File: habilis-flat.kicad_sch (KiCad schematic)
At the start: 73 parts, among them J1 AudioJack4, SW1 MX, SW10 MX, SW11 MX, SW12 MX, SW13 MX, SW14 MX, SW15 MX, SW16 MX, SW17 MX, SW18 MX, SW19 MX, SW2 MX, SW20 MX, SW21 MX, SW22 MX, SW23 MX, SW24 MX, SW25 MX, SW26 MX, SW27 MX, SW28 MX, SW29 MX, SW3 MX, SW31 MX, SW32 MX, SW33 MX, SW34 MX, SW35 MX, SW36 MX, SW4 MX, SW5 MX, SW6 MX, SW7 MX, SW8 MX, SW9 MX, U1 ProMicro

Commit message: Revision 1
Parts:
- removed D36: 1N4148, Diode_THT:D_DO-35_SOD27_P7.62mm_Horizontal, symbol Diode:1N4148
- added D35: 1N4148, Diode_THT:D_DO-35_SOD27_P7.62mm_Horizontal, symbol Diode:1N4148
- renumbered D31 to D30, D32 to D31, D33 to D32, D34 to D33, D35 to D34, SW31 to SW30, SW32 to SW31, SW33 to SW32, SW34 to SW33, SW35 to SW34, SW36 to SW35
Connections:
- net at D14.1 (K), D19.1 (K), D24.1 (K)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: now also D34.1 (K); no longer D33.1 (K)
- net at D10.1 (K), D15.1 (K), D20.1 (K)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: now also D30.1 (K), D35.1 (K); no longer D34.1 (K)
- net at SW26.2, SW27.2, SW28.2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: now also SW30.2
- net at D1.1 (K), D11.1 (K), D16.1 (K)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: now also D31.1 (K); no longer D30.1 (K)
- net at J1.S: no longer U1.5 (SDA)
- net at SW31.2, SW32.2, SW34.2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: now also SW33.1, U1.18 (F6); no longer SW30.2, SW33.2, U1.19 (F5)
- net at D12.1 (K), D17.1 (K), D2.1 (K)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: now also D32.1 (K); no longer D31.1 (K)
- net at SW35.1: now also D35.2 (A)
- net at D13.1 (K), D18.1 (K), D23.1 (K)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: now also D33.1 (K); no longer D32.1 (K)
- net at D33.2 (A): now also SW33.2; no longer SW33.1
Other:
- moved on the sheet: D30, D31, D32, D33, D34, SW30, SW31, SW32, SW33, SW34, SW35

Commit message: Revision 2
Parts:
- J1: footprint Connector_PinHeader_2.54mm:PinHeader_1x04_P2.54mm_Vertical -> project-components:Jack breakout board
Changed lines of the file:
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@@
       (effects (font (size 1.27 1.27)))
     )
-    (property "Footprint" "Connector_PinHeader_2.54mm:PinHeader_1x04_P2.54mm_Vertical" (at 85.09 120.65 0)
+    (property "Footprint" "project-components:Jack breakout board" (at 85.09 120.65 0)
       (effects (font (size 1.27 1.27)) hide)
     )

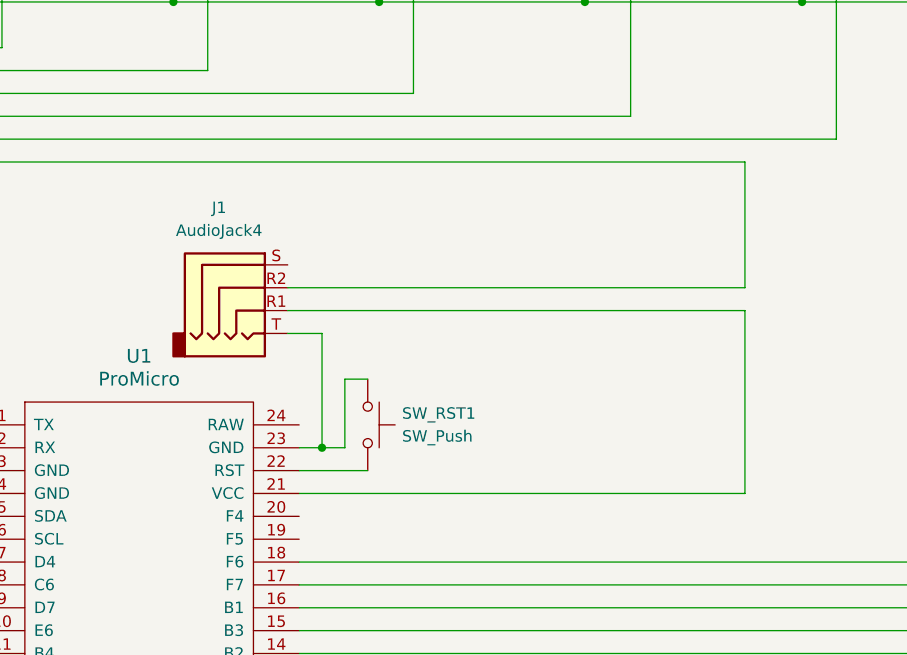
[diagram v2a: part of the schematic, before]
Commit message: Merge R1 and R2 of the TRRS
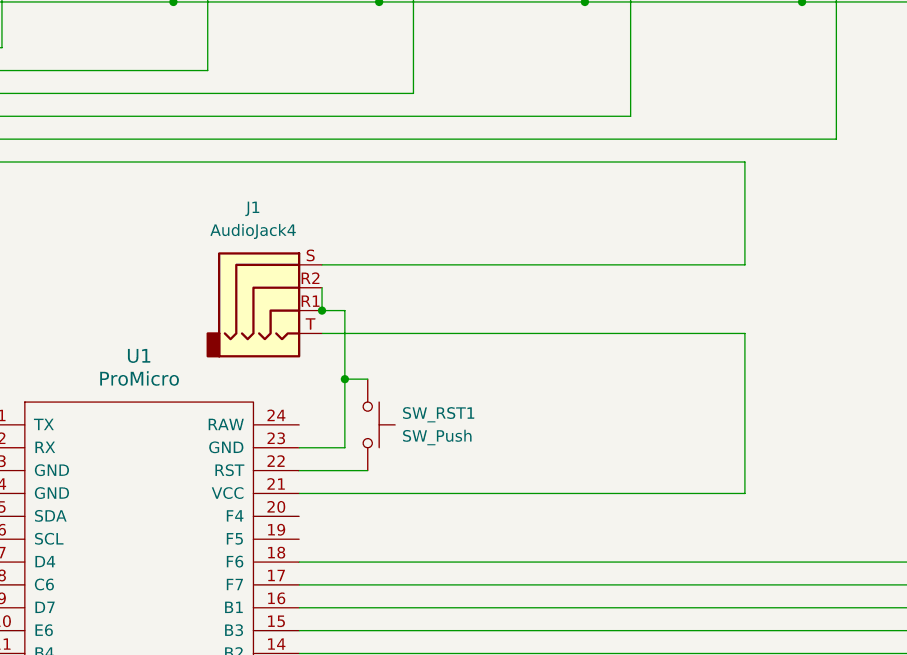
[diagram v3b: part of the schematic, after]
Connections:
- net at J1.R1: now also J1.R2, SW_RST1.1, U1.23 (GND); no longer U1.21 (VCC)
- net at U1.6 (SCL): now also J1.S; no longer J1.R2
- new net: J1.T, U1.21 (VCC)
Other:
- moved on the sheet: J1
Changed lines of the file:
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@@
 (kicad_sch (version 20230121) (generator eeschema)
   (paper "A4")
+  (junction (at 93.98 123.19) (diameter 0) (color 0 0 0 0)
+  )
   (junction (at 104.14 85.09) (diameter 0) (color 0 0 0 0)
   )
@@
   (junction (at 170.18 49.53) (diameter 0) (color 0 0 0 0)
   )
+  (junction (at 96.52 130.81) (diameter 0) (color 0 0 0 0)
+  )
   (junction (at 193.04 49.53) (diameter 0) (color 0 0 0 0)
   )
@@
   (junction (at 81.28 85.09) (diameter 0) (color 0 0 0 0)
   )
-  (junction (at 93.98 138.43) (diameter 0) (color 0 0 0 0)
-  )
   (junction (at 58.42 85.09) (diameter 0) (color 0 0 0 0)
   )
@@
     (stroke (width 0) (type default))
   )
-  (wire (pts (xy 140.97 143.51) (xy 140.97 123.19))
-    (stroke (width 0) (type default))
-  )
   (wire (pts (xy 77.47 58.42) (xy 77.47 62.23))
     (stroke (width 0) (type default))
@@
     (stroke (width 0) (type default))
   )
-  (wire (pts (xy 91.44 138.43) (xy 93.98 138.43))
+  (wire (pts (xy 91.44 138.43) (xy 96.52 138.43))
     (stroke (width 0) (type default))
   )
@@
     (stroke (width 0) (type default))
   )
+  (wire (pts (xy 96.52 130.81) (xy 96.52 138.43))
+    (stroke (width 0) (type default))
+  )
   (wire (pts (xy 193.04 36.83) (xy 203.2 36.83))
     (stroke (width 0) (type default))
@@
     (stroke (width 0) (type default))
   )
-  (wire (pts (xy 93.98 125.73) (xy 90.17 125.73))
-    (stroke (width 0) (type default))
-  )
   (wire (pts (xy 45.72 101.6) (xy 128.27 101.6))
     (stroke (width 0) (type default))
@@
     (stroke (width 0) (type default))
   )
+  (wire (pts (xy 93.98 120.65) (xy 93.98 123.19))
+    (stroke (width 0) (type default))
+  )
   (wire (pts (xy 100.33 85.09) (xy 100.33 88.9))
     (stroke (width 0) (type default))
@@
     (stroke (width 0) (type default))
   )
+  (wire (pts (xy 93.98 123.19) (xy 96.52 123.19))
+    (stroke (width 0) (type default))
+  )
   (wire (pts (xy 55.88 156.21) (xy 43.18 156.21))
     (stroke (width 0) (type default))
@@
     (stroke (width 0) (type default))
   )
-  (wire (pts (xy 140.97 106.68) (xy 140.97 120.65))
+  (wire (pts (xy 140.97 106.68) (xy 140.97 118.11))
     (stroke (width 0) (type default))
   )
@@
     (stroke (width 0) (type default))
   )
+  (wire (pts (xy 140.97 125.73) (xy 140.97 143.51))
+    (stroke (width 0) (type default))
+  )
   (wire (pts (xy 96.52 130.81) (xy 99.06 130.81))
     (stroke (width 0) (type default))
@@
     (stroke (width 0) (type default))
   )
-  (wire (pts (xy 93.98 138.43) (xy 93.98 125.73))
-    (stroke (width 0) (type default))
-  )
   (wire (pts (xy 45.72 58.42) (xy 46.99 58.42))
     (stroke (width 0) (type default))
@@
     (stroke (width 0) (type default))
   )
-  (wire (pts (xy 90.17 120.65) (xy 140.97 120.65))
+  (wire (pts (xy 93.98 118.11) (xy 140.97 118.11))
     (stroke (width 0) (type default))
   )
@@
     (stroke (width 0) (type default))
   )
+  (wire (pts (xy 96.52 123.19) (xy 96.52 130.81))
+    (stroke (width 0) (type default))
+  )
   (wire (pts (xy 91.44 163.83) (xy 203.2 163.83))
     (stroke (width 0) (type default))
@@
     (stroke (width 0) (type default))
   )
-  (wire (pts (xy 93.98 138.43) (xy 96.52 138.43))
+  (wire (pts (xy 93.98 125.73) (xy 140.97 125.73))
     (stroke (width 0) (type default))
   )
@@
     (stroke (width 0) (type default))
   )
-  (wire (pts (xy 140.97 123.19) (xy 90.17 123.19))
-    (stroke (width 0) (type default))
-  )
   (wire (pts (xy 77.47 71.12) (xy 77.47 74.93))
     (stroke (width 0) (type default))
@@
   )
   (wire (pts (xy 147.32 74.93) (xy 123.19 74.93))
-    (stroke (width 0) (type default))
-  )
-  (wire (pts (xy 96.52 138.43) (xy 96.52 130.81))
     (stroke (width 0) (type default))
   )
@@
     )
   )
-  (symbol (lib_id "Connector_Audio:AudioJack4") (at 85.09 120.65 0) (unit 1)
-    (in_bom yes) (on_board yes) (dnp no) (fields_autoplaced)
-    (property "Reference" "J1" (at 82.55 111.76 0)
-      (effects (font (size 1.27 1.27)))
-    )
-    (property "Value" "AudioJack4" (at 82.55 114.3 0)
-      (effects (font (size 1.27 1.27)))
-    )
-    (property "Footprint" "project-components:Jack breakout board" (at 85.09 120.65 0)
-      (effects (font (size 1.27 1.27)) hide)
-    )
-    (property "Datasheet" "~" (at 85.09 120.65 0)
-      (effects (font (size 1.27 1.27)) hide)
-    )
+  (symbol (lib_id "Connector_Audio:AudioJack4") (at 88.9 120.65 0) (unit 1)
+    (in_bom yes) (on_board yes) (dnp no)
+    (property "Reference" "J1" (at 86.36 111.76 0)
+      (effects (font (size 1.27 1.27)))
+    )
+    (property "Value" "AudioJack4" (at 86.36 114.3 0)
+      (effects (font (size 1.27 1.27)))
+    )
+    (property "Footprint" "project-components:Jack breakout board" (at 88.9 120.65 0)
+      (effects (font (size 1.27 1.27)) hide)
+    )
+    (property "Datasheet" "~" (at 88.9 120.65 0)
+      (effects (font (size 1.27 1.27)) hide)
+    )

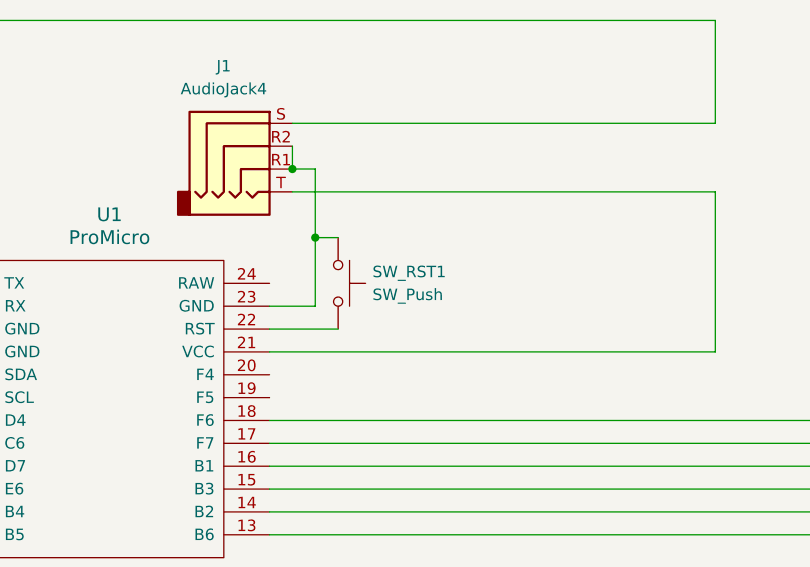
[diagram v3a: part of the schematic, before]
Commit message: Put reset switch on the opposite side
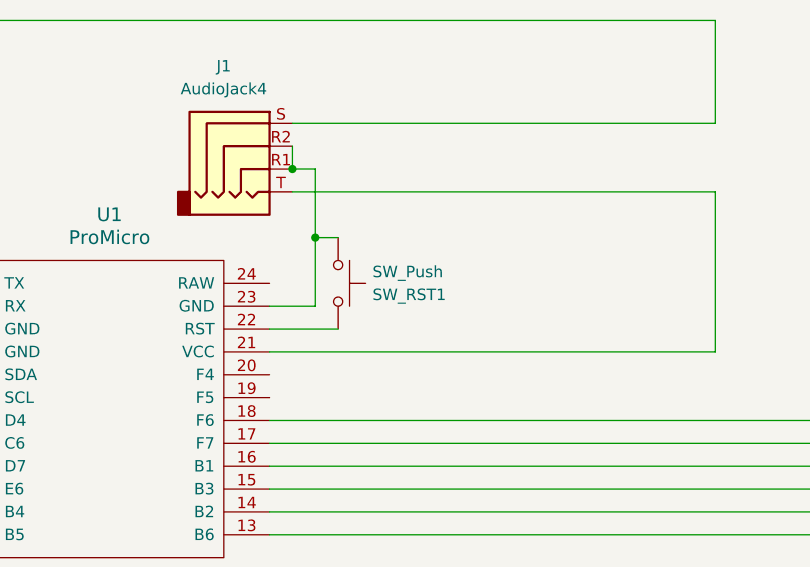
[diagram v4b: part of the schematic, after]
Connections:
- net at J1.R1, J1.R2, U1.23 (GND): now also SW_RST1.2; no longer SW_RST1.1
- net at U1.22 (RST): now also SW_RST1.1; no longer SW_RST1.2
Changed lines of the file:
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@@
     )
   )
-  (symbol (lib_id "Switch:SW_Push") (at 99.06 135.89 270) (unit 1)
-    (in_bom yes) (on_board yes) (dnp no) (fields_autoplaced)
-    (property "Reference" "SW_RST1" (at 102.87 134.62 90)
+  (symbol (lib_id "Switch:SW_Push") (at 99.06 135.89 270) (mirror x) (unit 1)
+    (in_bom yes) (on_board yes) (dnp no)
+    (property "Reference" "SW_RST1" (at 102.87 137.16 90)
       (effects (font (size 1.27 1.27)) (justify left))
     )
-    (property "Value" "SW_Push" (at 102.87 137.16 90)
+    (property "Value" "SW_Push" (at 102.87 134.62 90)
       (effects (font (size 1.27 1.27)) (justify left))
     )

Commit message: Replace MX footprint with reversible version
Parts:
- SW1, SW10, SW11, SW12, SW13, SW14, SW15, SW16, SW17, SW18, SW19, SW2, SW20, SW21, SW22, SW23, SW24, SW25, SW26, SW27, SW28, SW29, SW3, SW30, SW31, SW32, SW33, SW34, SW35, SW4, SW5, SW6, SW7, SW8, SW9: footprint Button_Switch_Keyboard:SW_Cherry_MX_1.00u_PCB -> project-components:SW_MX_reversible_decentered

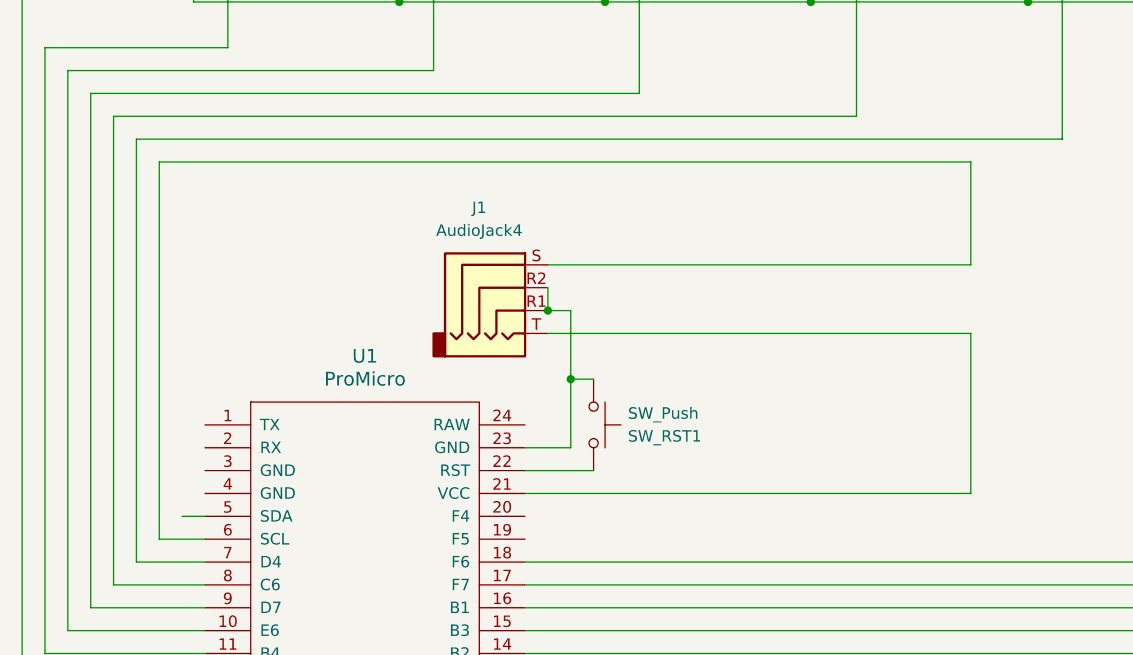
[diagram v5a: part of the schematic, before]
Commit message: Duplicate TRRS header
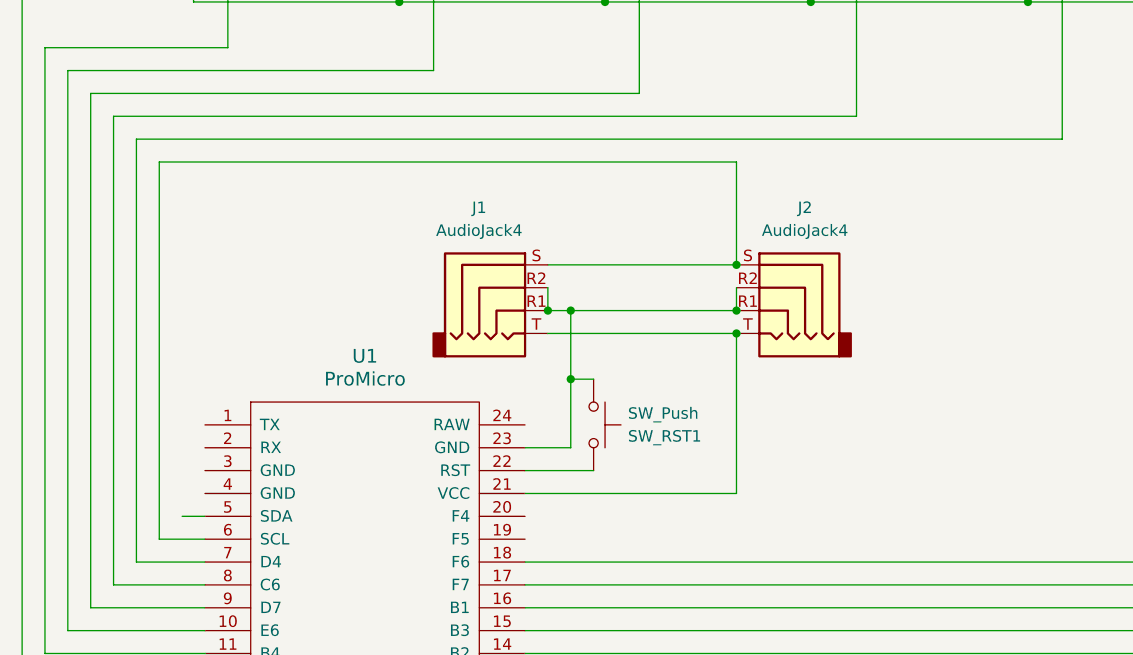
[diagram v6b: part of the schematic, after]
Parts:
- added J2: AudioJack4, project-components:Jack breakout board, symbol Connector_Audio:AudioJack4
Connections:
- net at J1.R1, J1.R2, SW_RST1.2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: now also J2.R1, J2.R2
- net at J1.S, U1.6 (SCL): now also J2.S
- net at J1.T, U1.21 (VCC): now also J2.T
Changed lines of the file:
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@@
   (junction (at 128.27 71.12) (diameter 0) (color 0 0 0 0)
   )
+  (junction (at 96.52 123.19) (diameter 0) (color 0 0 0 0)
+  )
   (junction (at 58.42 45.72) (diameter 0) (color 0 0 0 0)
   )
@@
   (junction (at 147.32 88.9) (diameter 0) (color 0 0 0 0)
   )
+  (junction (at 114.935 118.11) (diameter 0) (color 0 0 0 0)
+  )
   (junction (at 100.33 74.93) (diameter 0) (color 0 0 0 0)
   )
@@
   (junction (at 151.13 58.42) (diameter 0) (color 0 0 0 0)
   )
+  (junction (at 114.935 125.73) (diameter 0) (color 0 0 0 0)
+  )
   (junction (at 173.99 71.12) (diameter 0) (color 0 0 0 0)
   )
@@
   (junction (at 100.33 36.83) (diameter 0) (color 0 0 0 0)
   )
+  (junction (at 114.935 123.19) (diameter 0) (color 0 0 0 0)
+  )
   (wire (pts (xy 195.58 74.93) (xy 195.58 156.21))
     (stroke (width 0) (type default))
@@
     (stroke (width 0) (type default))
   )
+  (wire (pts (xy 114.935 120.65) (xy 114.935 123.19))
+    (stroke (width 0) (type default))
+  )
   (wire (pts (xy 38.1 161.29) (xy 38.1 93.98))
     (stroke (width 0) (type default))
@@
     (stroke (width 0) (type default))
   )
-  (wire (pts (xy 91.44 143.51) (xy 140.97 143.51))
-    (stroke (width 0) (type default))
-  )
-  (wire (pts (xy 140.97 106.68) (xy 140.97 118.11))
+  (wire (pts (xy 91.44 143.51) (xy 114.935 143.51))
+    (stroke (width 0) (type default))
+  )
+  (wire (pts (xy 114.935 106.68) (xy 114.935 118.11))
     (stroke (width 0) (type default))
   )
@@
     (stroke (width 0) (type default))
   )
-  (wire (pts (xy 140.97 125.73) (xy 140.97 143.51))
+  (wire (pts (xy 114.935 125.73) (xy 114.935 143.51))
     (stroke (width 0) (type default))
   )
@@
     (stroke (width 0) (type default))
   )
+  (wire (pts (xy 96.52 123.19) (xy 114.935 123.19))
+    (stroke (width 0) (type default))
+  )
   (wire (pts (xy 91.44 153.67) (xy 193.04 153.67))
     (stroke (width 0) (type default))
@@
     (stroke (width 0) (type default))
   )
-  (wire (pts (xy 93.98 118.11) (xy 140.97 118.11))
+  (wire (pts (xy 93.98 118.11) (xy 114.935 118.11))
     (stroke (width 0) (type default))
   )
@@
     (stroke (width 0) (type default))
   )
-  (wire (pts (xy 50.8 106.68) (xy 140.97 106.68))
+  (wire (pts (xy 50.8 106.68) (xy 114.935 106.68))
     (stroke (width 0) (type default))
   )
@@
     (stroke (width 0) (type default))
   )
-  (wire (pts (xy 93.98 125.73) (xy 140.97 125.73))
+  (wire (pts (xy 93.98 125.73) (xy 114.935 125.73))
     (stroke (width 0) (type default))
   )
@@
         )
       )
+    )
+  )
+  (symbol (lib_id "Connector_Audio:AudioJack4") (at 120.015 120.65 0) (mirror y) (unit 1)
+    (in_bom yes) (on_board yes) (dnp no)
+    (property "Reference" "J2" (at 122.555 111.76 0)
+      (effects (font (size 1.27 1.27)))
+    )
+    (property "Value" "AudioJack4" (at 122.555 114.3 0)
+      (effects (font (size 1.27 1.27)))
+    )
+    (property "Footprint" "project-components:Jack breakout board" (at 120.015 120.65 0)
+      (effects (font (size 1.27 1.27)) hide)
+    )
+    (property "Datasheet" "~" (at 120.015 120.65 0)
+      (effects (font (size 1.27 1.27)) hide)
+    )
+    (pin "R1")
+    (pin "R2")
+    (pin "S")
+    (pin "T")
+    (instances
+      (project "habilis-flat"
+        (path "/30459cb5-f789-45d2-9dbe-3bb0e13b9b1e"
+          (reference "J2") (unit 1)
+        )
+      )
